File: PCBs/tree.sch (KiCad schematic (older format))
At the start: 29 parts, among them SW1 SW_Push_DPDT, SW2 SW_SPST, U1 Shift_Reg, U2 Shift_Reg, U3 Shift_Reg

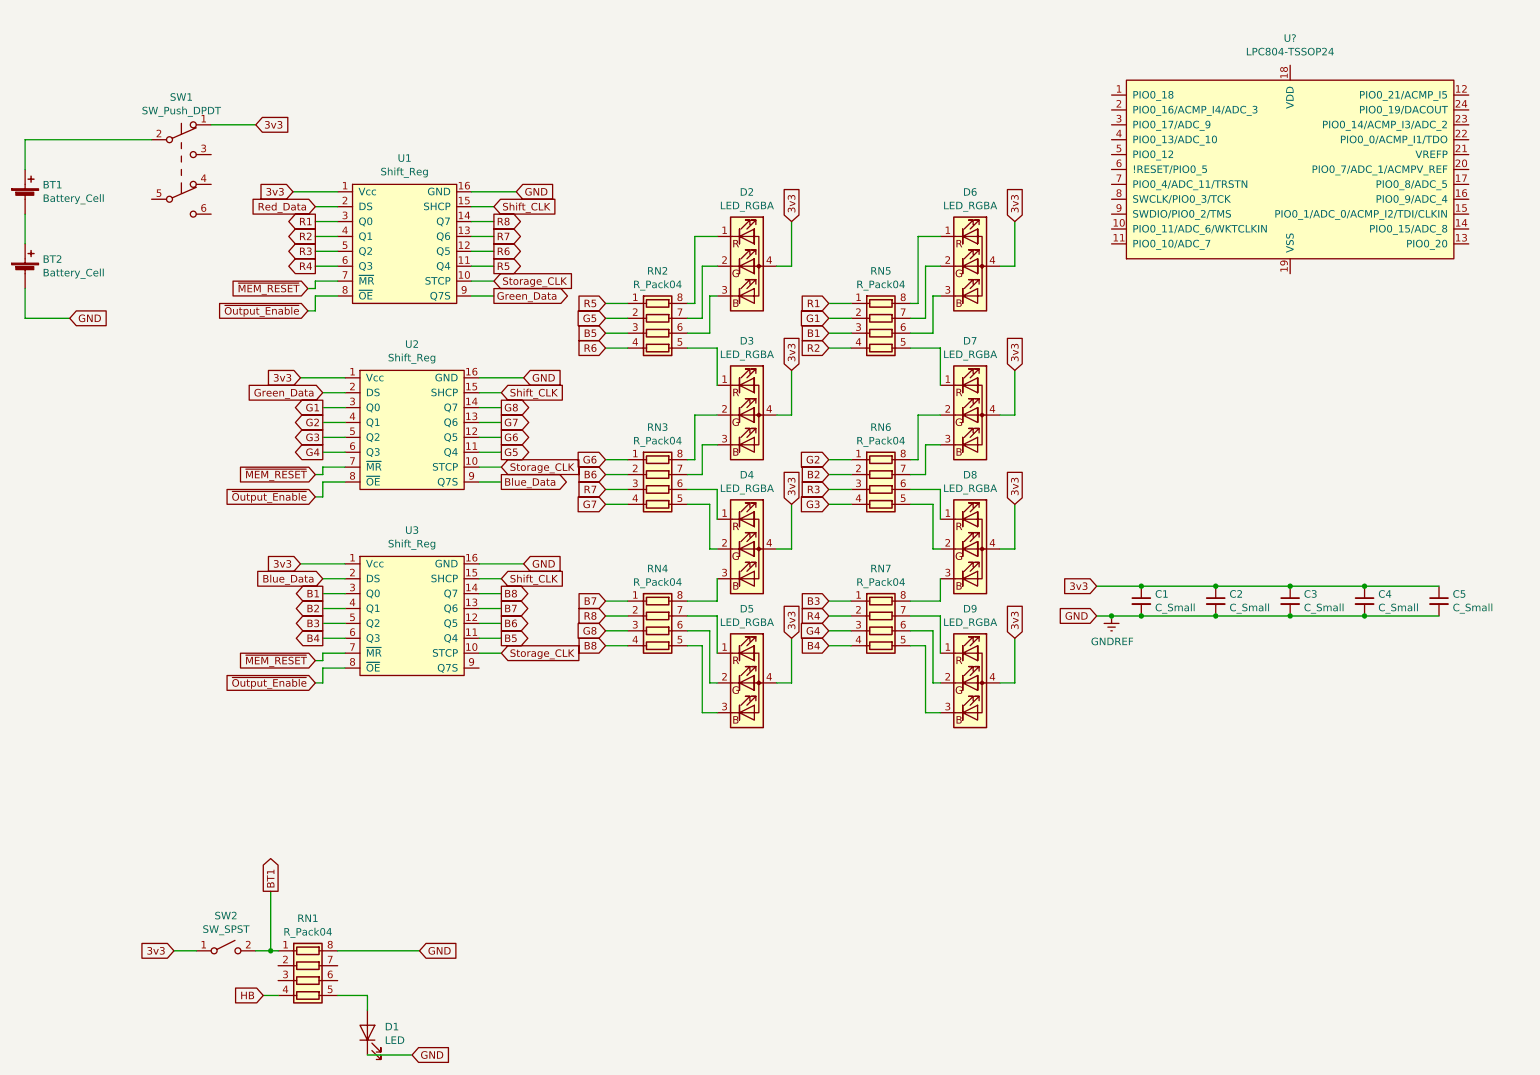
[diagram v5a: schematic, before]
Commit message: Addressing SWD header
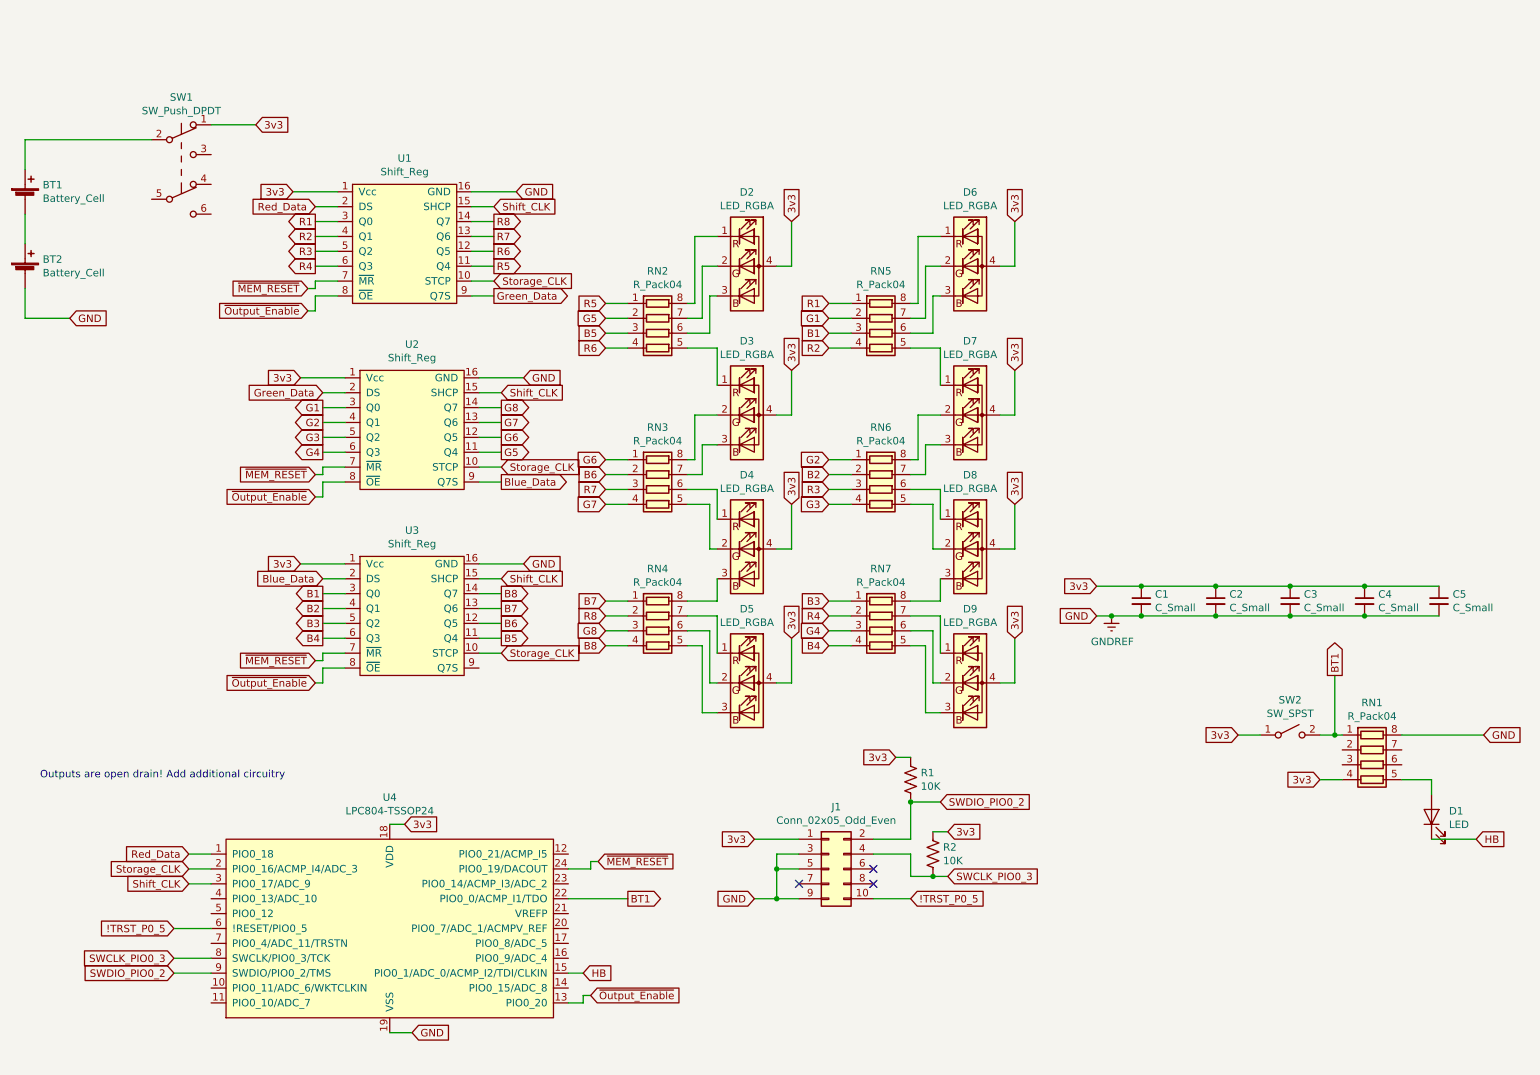
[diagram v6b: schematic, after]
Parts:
- added J1: Conn_02x05_Odd_Even, symbol Connector_Generic:Conn_02x05_Odd_Even
- added R1, R2: 10K, symbol Device:R_US
- gave numbers to parts that had none: 1
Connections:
- net 3v3: now also RN1.4 (R4.1), U4.18 (VDD), J1.1 (Pin_1), R1.1, R2.1
- net BT1: now also U4.22 (PIO0_0/ACMP_I1/TDO)
- net GNDREF: now also U4.19 (VSS), J1.3 (Pin_3), J1.5 (Pin_5), J1.9 (Pin_9); no longer D1.1 (K)
- net HB: now also D1.1 (K), U4.15 (PIO0_1/ADC_0/ACMP_I2/TDI/CLKIN); no longer RN1.4 (R4.1)
- net Red_Data: now also U4.1 (PIO0_18)
- net Shift_CLK: now also U4.3 (PIO0_17/ADC_9)
- net Storage_CLK: now also U4.2 (PIO0_16/ACMP_I4/ADC_3)
- net ~MEM_RESET~: now also U4.24 (PIO0_19/DACOUT)
- net ~Output_Enable~: now also U4.13 (PIO0_20)
- net !TRST_P0_5: now reaches U4.6 (!RESET/PIO0_5)
- net !TRST_P0_5: now also J1.10 (Pin_10)
- net SWCLK_PIO0_3: now reaches U4.8 (SWCLK/PIO0_3/TCK)
- net SWCLK_PIO0_3: now also J1.4 (Pin_4), R2.2
- net SWDIO_PIO0_2: now reaches U4.9 (SWDIO/PIO0_2/TMS)
- net SWDIO_PIO0_2: now also J1.2 (Pin_2), R1.2
- no-connect marks 0 -> 3
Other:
- note added: "Outputs are open drain! Add additional circuitry"
- moved on the sheet: D1, RN1, SW2, U4
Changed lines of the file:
@@
 L Device:LED D1
 U 1 1 6032CD9A
-P 3300 7300
-F 0 "D1" V 3339 7183 50  0000 R CNN
-F 1 "LED" V 3248 7183 50  0000 R CNN
-F 2 "LED_SMD:LED_0603_1608Metric_Pad1.05x0.95mm_HandSolder" H 3300 7300 50  0001 C CNN
-F 3 "~" H 3300 7300 50  0001 C CNN
-	1    3300 7300
+P 10450 5850
+F 0 "D1" V 10489 5733 50  0000 R CNN
+F 1 "LED" V 10398 5733 50  0000 R CNN
+F 2 "LED_SMD:LED_0603_1608Metric_Pad1.05x0.95mm_HandSolder" H 10450 5850 50  0001 C CNN
+F 3 "~" H 10450 5850 50  0001 C CNN
+	1    10450 5850
 	0    -1   -1   0
 $EndComp
-Text GLabel 2600 7050 0    50   Input ~ 0
-HB
-Wire Wire Line
-	2600 7050 2700 7050
-Wire Wire Line
-	3300 7050 3300 7150
+Wire Wire Line
+	10450 5600 10450 5700
 Text GLabel 2950 1750 0    50   Input ~ 0
 Red_Data
@@
 L Device:R_Pack04 RN1
 U 1 1 602C2C14
-P 2900 6950
-F 0 "RN1" V 2483 6950 50  0000 C CNN
-F 1 "R_Pack04" V 2574 6950 50  0000 C CNN
-F 2 "Resistor_SMD:R_Array_Convex_4x0603" V 3175 6950 50  0001 C CNN
-F 3 "~" H 2900 6950 50  0001 C CNN
-	1    2900 6950
+P 10050 5500
+F 0 "RN1" V 9633 5500 50  0000 C CNN
+F 1 "R_Pack04" V 9724 5500 50  0000 C CNN
+F 2 "Resistor_SMD:R_Array_Convex_4x0603" V 10325 5500 50  0001 C CNN
+F 3 "~" H 10050 5500 50  0001 C CNN
+	1    10050 5500
 	0    1    1    0
 $EndComp
 Wire Wire Line
-	3300 7050 3100 7050
-Text GLabel 3600 7450 2    50   Input ~ 0
-GND
-Wire Wire Line
-	3600 7450 3300 7450
-Text GLabel 2000 6750 0    50   Input ~ 0
-3v3
-Wire Wire Line
-	2000 6750 2150 6750
+	10450 5600 10250 5600
+Text GLabel 10750 6000 2    50   Input ~ 0
+HB
+Wire Wire Line
+	10750 6000 10450 6000
+Text GLabel 9150 5300 0    50   Input ~ 0
+3v3
+Wire Wire Line
+	9150 5300 9300 5300
 $Comp
 L Switch:SW_SPST SW2
 U 1 1 6037EFD6
-P 2350 6750
-F 0 "SW2" H 2350 6985 50  0000 C CNN
-F 1 "SW_SPST" H 2350 6894 50  0000 C CNN
-F 2 "LL3301FF065QJ_pushbutton:LL3301FF065QJ" H 2350 6750 50  0001 C CNN
-F 3 "~" H 2350 6750 50  0001 C CNN
-	1    2350 6750
-	1    0    0    -1
-$EndComp
-Text GLabel 3650 6750 2    50   Input ~ 0
+P 9500 5300
+F 0 "SW2" H 9500 5535 50  0000 C CNN
+F 1 "SW_SPST" H 9500 5444 50  0000 C CNN
+F 2 "LL3301FF065QJ_pushbutton:LL3301FF065QJ" H 9500 5300 50  0001 C CNN
+F 3 "~" H 9500 5300 50  0001 C CNN
+	1    9500 5300
+	1    0    0    -1
+$EndComp
+Text GLabel 10800 5300 2    50   Input ~ 0
 GND
-Text GLabel 2650 6350 1    50   Output ~ 0
+Text GLabel 9800 4900 1    50   Output ~ 0
 BT1
 Wire Wire Line
-	3100 6750 3650 6750
-Wire Wire Line
-	2700 6750 2650 6750
-Wire Wire Line
-	2650 6350 2650 6750
-Connection ~ 2650 6750
-Wire Wire Line
-	2650 6750 2550 6750
-$Comp
-L MCU_NXP_LPC804:LPC804-TSSOP24 U?
+	10250 5300 10800 5300
+Wire Wire Line
+	9850 5300 9800 5300
+Wire Wire Line
+	9800 4900 9800 5300
+Connection ~ 9800 5300
+Wire Wire Line
+	9800 5300 9700 5300
+$Comp
+L MCU_NXP_LPC804:LPC804-TSSOP24 U4
 U 1 1 6024220D
-P 9500 1450
-F 0 "U?" H 9500 2281 50  0000 C CNN
-F 1 "LPC804-TSSOP24" H 9500 2190 50  0000 C CNN
-F 2 "" H 8800 1450 50  0001 C CNN
-F 3 "" H 8800 1450 50  0001 C CNN
-	1    9500 1450
-	1    0    0    -1
-$EndComp
+P 3450 6550
+F 0 "U4" H 3450 7381 50  0000 C CNN
+F 1 "LPC804-TSSOP24" H 3450 7290 50  0000 C CNN
+F 2 "" H 2750 6550 50  0001 C CNN
+F 3 "" H 2750 6550 50  0001 C CNN
+	1    3450 6550
+	1    0    0    -1
+$EndComp
+$Comp
+L Connector_Generic:Conn_02x05_Odd_Even J1
+U 1 1 6022D914
+P 6400 6200
+F 0 "J1" H 6450 6617 50  0000 C CNN
+F 1 "Conn_02x05_Odd_Even" H 6450 6526 50  0000 C CNN
+F 2 "" H 6400 6200 50  0001 C CNN
+F 3 "~" H 6400 6200 50  0001 C CNN
+	1    6400 6200
+	1    0    0    -1
+$EndComp
+Text GLabel 5900 6000 0    50   Input ~ 0
+3v3
+Wire Wire Line
+	5900 6000 6200 6000
+Text GLabel 5900 6400 0    50   Input ~ 0
+GND
+Wire Wire Line
+	5900 6400 6050 6400
+NoConn ~ 6200 6300
+Wire Wire Line
+	6200 6100 6050 6100
+Wire Wire Line
+	6050 6100 6050 6200
+Connection ~ 6050 6400
+Wire Wire Line
+	6050 6400 6200 6400
+Wire Wire Line
+	6200 6200 6050 6200
+Connection ~ 6050 6200
+Wire Wire Line
+	6050 6200 6050 6400
+NoConn ~ 6700 6200
+NoConn ~ 6700 6300
+Text GLabel 7150 5750 2    50   Input ~ 0
+SWDIO_PIO0_2
+Wire Wire Line
+	6700 6000 6950 6000
+Text GLabel 7200 6250 2    50   Input ~ 0
+SWCLK_PIO0_3
+Wire Wire Line
+	6700 6100 6950 6100
+Text GLabel 6950 6400 2    50   Input ~ 0
+!TRST_P0_5
+Wire Wire Line
+	6700 6400 6950 6400
+Text GLabel 2000 6900 0    50   Input ~ 0
+SWDIO_PIO0_2
+Wire Wire Line
+	2250 6900 2000 6900
+Text GLabel 2000 6800 0    50   Input ~ 0
+SWCLK_PIO0_3
+Wire Wire Line
+	2250 6800 2000 6800
+Text GLabel 2000 6600 0    50   Input ~ 0
+!TRST_P0_5
+Wire Wire Line
+	2250 6600 2000 6600
+Wire Wire Line
+	6950 6000 6950 5750
+Wire Wire Line
+	6950 5750 7150 5750
+$Comp
+L Device:R_US R1
+U 1 1 6031BFCF
+P 6950 5600
+F 0 "R1" H 7018 5646 50  0000 L CNN
+F 1 "10K" H 7018 5555 50  0000 L CNN
+F 2 "" V 6990 5590 50  0001 C CNN
+F 3 "~" H 6950 5600 50  0001 C CNN
+	1    6950 5600
+	1    0    0    -1
+$EndComp
+Connection ~ 6950 5750
+Wire Wire Line
+	6950 6100 6950 6250
+Wire Wire Line
+	6950 6250 7100 6250
+$Comp
+L Device:R_US R2
+U 1 1 6032D2AD
+P 7100 6100
+F 0 "R2" H 7168 6146 50  0000 L CNN
+F 1 "10K" H 7168 6055 50  0000 L CNN
+F 2 "" V 7140 6090 50  0001 C CNN
+F 3 "~" H 7100 6100 50  0001 C CNN
+	1    7100 6100
+	1    0    0    -1
+$EndComp
+Text GLabel 6850 5450 0    50   Input ~ 0
+3v3
+Wire Wire Line
+	6850 5450 6950 5450
+Text GLabel 7200 5950 2    50   Input ~ 0
+3v3
+Wire Wire Line
+	7200 5950 7100 5950
+Connection ~ 7100 6250
+Wire Wire Line
+	7100 6250 7200 6250
+Text GLabel 3550 5900 2    50   Input ~ 0
+3v3
+Wire Wire Line
+	3550 5900 3450 5900
+Text GLabel 3600 7300 2    50   Input ~ 0
+GND
+Wire Wire Line
+	3600 7300 3450 7300
+Text GLabel 2100 6100 0    50   Input ~ 0
+Red_Data
+Wire Wire Line
+	2100 6100 2250 6100
+Text GLabel 2100 6300 0    50   Input ~ 0
+Shift_CLK
+Wire Wire Line
+	2100 6300 2250 6300
+Text GLabel 2100 6200 0    50   Input ~ 0
+Storage_CLK
+Wire Wire Line
+	2100 6200 2250 6200
+Text GLabel 4850 6150 2    50   Input ~ 0
+~MEM_RESET~
+Wire Wire Line
+	4850 6150 4800 6150
+Wire Wire Line
+	4800 6150 4800 6200
+Wire Wire Line
+	4800 6200 4650 6200
+Text GLabel 4800 7050 2    50   Input ~ 0
+~Output_Enable~
+Wire Wire Line
+	4800 7050 4750 7050
+Wire Wire Line
+	4750 7050 4750 7100
+Wire Wire Line
+	4650 7100 4750 7100
+Text GLabel 5050 6400 2    50   Output ~ 0
+BT1
+Wire Wire Line
+	5050 6400 4650 6400
+Text GLabel 4750 6900 2    50   Input ~ 0
+HB
+Wire Wire Line
+	4750 6900 4650 6900
+Text GLabel 9700 5600 0    50   Input ~ 0
+3v3
+Wire Wire Line
+	9700 5600 9850 5600
+Text Notes 1100 5600 0    50   ~ 0
+Outputs are open drain! Add additional circuitry
 $EndSCHEMATC

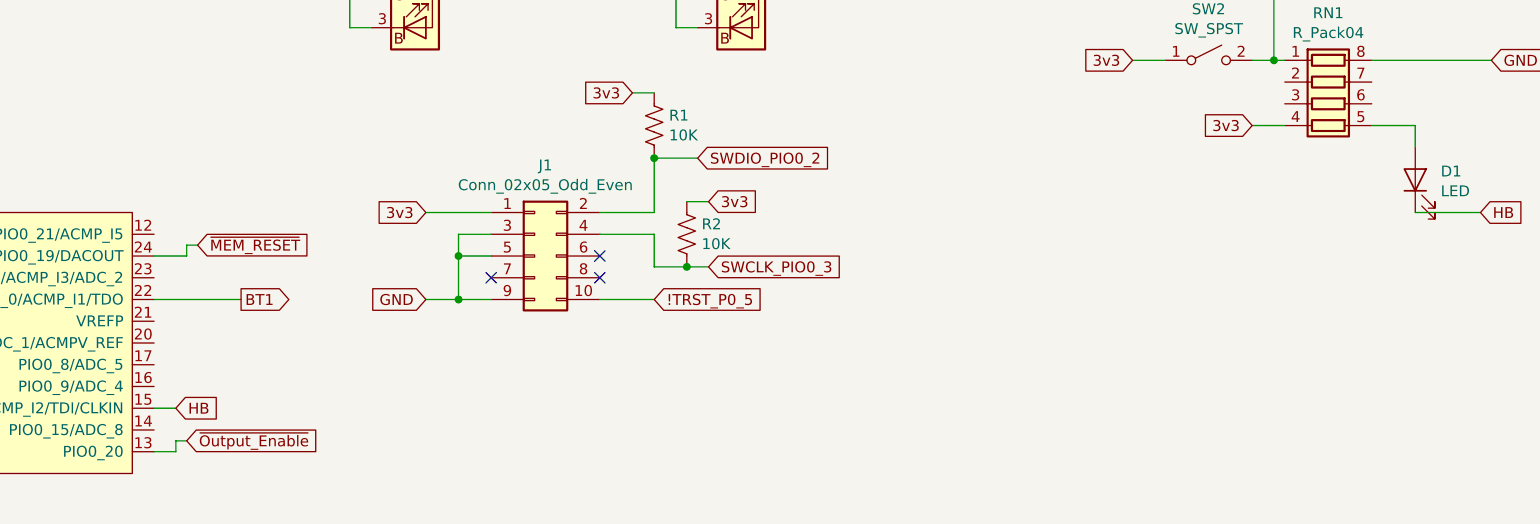
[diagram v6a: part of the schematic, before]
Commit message: Laid out a board with debug header and LPC804
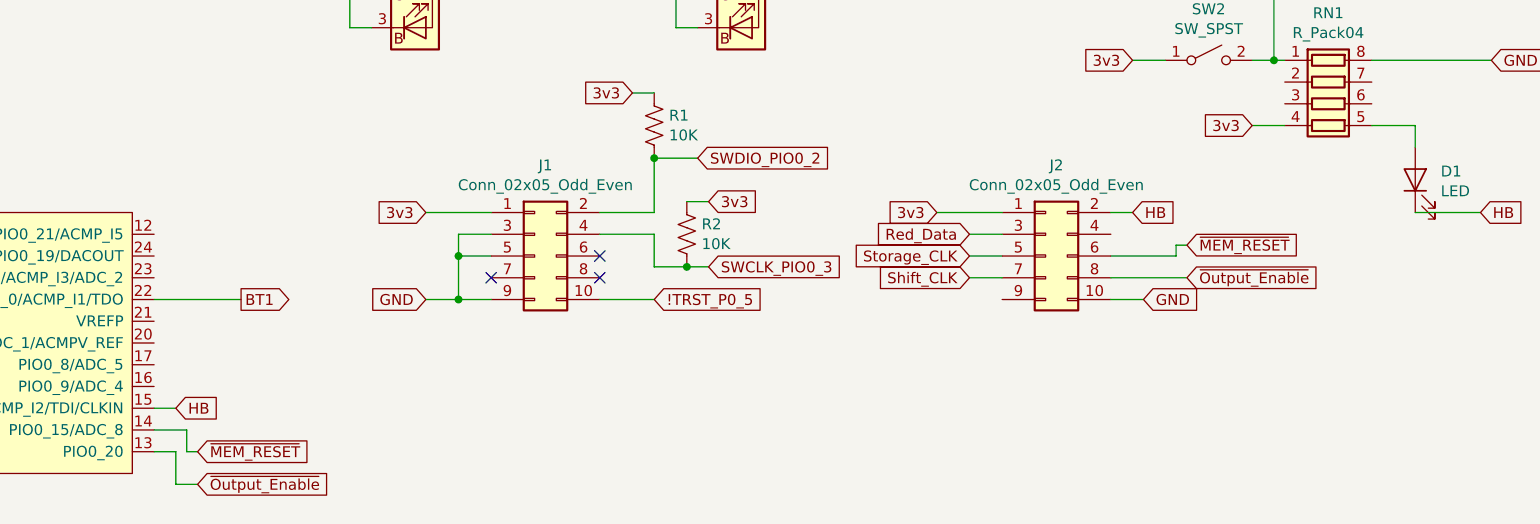
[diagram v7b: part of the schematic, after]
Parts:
- added J2: Conn_02x05_Odd_Even, Connector_PinHeader_2.54mm:PinHeader_2x05_P2.54mm_Vertical, symbol Connector_Generic:Conn_02x05_Odd_Even
- J1: footprint (none) -> Connector_PinHeader_1.27mm:PinHeader_2x05_P1.27mm_Vertical
- R1, R2: footprint (none) -> Resistor_SMD:R_0805_2012Metric
- U4: footprint (none) -> Package_SO:TSSOP-24_4.4x7.8mm_P0.65mm
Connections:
- net 3v3: now also J2.1 (Pin_1)
- net GNDREF: now also J2.10 (Pin_10)
- net HB: now also J2.2 (Pin_2)
- net Red_Data: now also J2.3 (Pin_3)
- net Shift_CLK: now also J2.7 (Pin_7)
- net Storage_CLK: now also J2.5 (Pin_5)
- net ~MEM_RESET~: now also U4.14 (PIO0_15/ADC_8), J2.6 (Pin_6); no longer U4.24 (PIO0_19/DACOUT)
- net ~Output_Enable~: now also J2.8 (Pin_8)
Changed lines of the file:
@@
 F 0 "U4" H 3450 7381 50  0000 C CNN
 F 1 "LPC804-TSSOP24" H 3450 7290 50  0000 C CNN
-F 2 "" H 2750 6550 50  0001 C CNN
+F 2 "Package_SO:TSSOP-24_4.4x7.8mm_P0.65mm" H 2750 6550 50  0001 C CNN
 F 3 "" H 2750 6550 50  0001 C CNN
 	1    3450 6550
@@
 F 0 "J1" H 6450 6617 50  0000 C CNN
 F 1 "Conn_02x05_Odd_Even" H 6450 6526 50  0000 C CNN
-F 2 "" H 6400 6200 50  0001 C CNN
+F 2 "Connector_PinHeader_1.27mm:PinHeader_2x05_P1.27mm_Vertical" H 6400 6200 50  0001 C CNN
 F 3 "~" H 6400 6200 50  0001 C CNN
 	1    6400 6200
@@
 F 0 "R1" H 7018 5646 50  0000 L CNN
 F 1 "10K" H 7018 5555 50  0000 L CNN
-F 2 "" V 6990 5590 50  0001 C CNN
+F 2 "Resistor_SMD:R_0805_2012Metric" V 6990 5590 50  0001 C CNN
 F 3 "~" H 6950 5600 50  0001 C CNN
 	1    6950 5600
@@
 F 0 "R2" H 7168 6146 50  0000 L CNN
 F 1 "10K" H 7168 6055 50  0000 L CNN
-F 2 "" V 7140 6090 50  0001 C CNN
+F 2 "Resistor_SMD:R_0805_2012Metric" V 7140 6090 50  0001 C CNN
 F 3 "~" H 7100 6100 50  0001 C CNN
 	1    7100 6100
@@
 Wire Wire Line
 	2100 6200 2250 6200
-Text GLabel 4850 6150 2    50   Input ~ 0
+Text GLabel 4850 7100 2    50   Input ~ 0
 ~MEM_RESET~
 Wire Wire Line
-	4850 6150 4800 6150
-Wire Wire Line
-	4800 6150 4800 6200
-Wire Wire Line
-	4800 6200 4650 6200
-Text GLabel 4800 7050 2    50   Input ~ 0
+	4850 7100 4800 7100
+Wire Wire Line
+	4800 7100 4800 7000
+Wire Wire Line
+	4800 7000 4650 7000
+Text GLabel 4850 7250 2    50   Input ~ 0
 ~Output_Enable~
 Wire Wire Line
-	4800 7050 4750 7050
-Wire Wire Line
-	4750 7050 4750 7100
+	4850 7250 4750 7250
+Wire Wire Line
+	4750 7250 4750 7100
 Wire Wire Line
 	4650 7100 4750 7100
@@
 Text Notes 1100 5600 0    50   ~ 0
 Outputs are open drain! Add additional circuitry
+$Comp
+L Connector_Generic:Conn_02x05_Odd_Even J2
+U 1 1 602498E0
+P 8750 6200
+F 0 "J2" H 8800 6617 50  0000 C CNN
+F 1 "Conn_02x05_Odd_Even" H 8800 6526 50  0000 C CNN
+F 2 "Connector_PinHeader_2.54mm:PinHeader_2x05_P2.54mm_Vertical" H 8750 6200 50  0001 C CNN
+F 3 "~" H 8750 6200 50  0001 C CNN
+	1    8750 6200
+	1    0    0    -1
+$EndComp
+Text GLabel 8400 6100 0    50   Input ~ 0
+Red_Data
+Wire Wire Line
+	8400 6100 8550 6100
+Text GLabel 8400 6300 0    50   Input ~ 0
+Shift_CLK
+Wire Wire Line
+	8400 6300 8550 6300
+Text GLabel 8400 6200 0    50   Input ~ 0
+Storage_CLK
+Wire Wire Line
+	8400 6200 8550 6200
+Text GLabel 9150 6000 2    50   Input ~ 0
+HB
+Wire Wire Line
+	9150 6000 9050 6000
+Text GLabel 9200 6400 2    50   Input ~ 0
+GND
+Wire Wire Line
+	9200 6400 9050 6400
+Text GLabel 8250 6000 0    50   Input ~ 0
+3v3
+Wire Wire Line
+	8250 6000 8550 6000
+Text GLabel 9400 6300 2    50   Input ~ 0
+~Output_Enable~
+Wire Wire Line
+	9050 6300 9400 6300
+Text GLabel 9400 6150 2    50   Input ~ 0
+~MEM_RESET~
+Wire Wire Line
+	9400 6150 9350 6150
+Wire Wire Line
+	9350 6150 9350 6200
+Wire Wire Line
+	9350 6200 9050 6200
 $EndSCHEMATC
